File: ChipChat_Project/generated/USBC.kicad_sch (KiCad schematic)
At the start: 4 parts

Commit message: 💾 snapshot 2026-02-23_00-19-22
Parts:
- added D1, D2, D3, D4, D5: TVS 5V, symbol SD05_SOD323
- added FB1: 120Ω@100MHz, symbol FerriteBead
- added J1: USB_C_Receptacle_USB2.0_16P, symbol USB_C_Receptacle_USB2.0_16P
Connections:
- net GND: now also D1.2 (A2), D2.2 (A2), D3.2 (A2), D4.2 (A2), D5.2 (A2), J1.A1 (GND), J1.A12 (GND), J1.B1 (GND), J1.B12 (GND), J1.S1 (SHIELD)
- net PP_5V_VBUS: now also D5.1 (A1), FB1.2, J1.A4 (VBUS), J1.A9 (VBUS), J1.B4 (VBUS), J1.B9 (VBUS)
- net USB_CC1: now also D4.1 (A1), J1.A5 (CC1)
- net USB_CC2: now also J1.B5 (CC2)
- new net PP_5V_SYS: FB1.1
- new net USB_DN: D1.1 (A1), D2.1 (A1), J1.A7 (D-), J1.B7 (D-)
- new net USB_DP: D3.1 (A1), J1.A6 (D+), J1.B6 (D+)

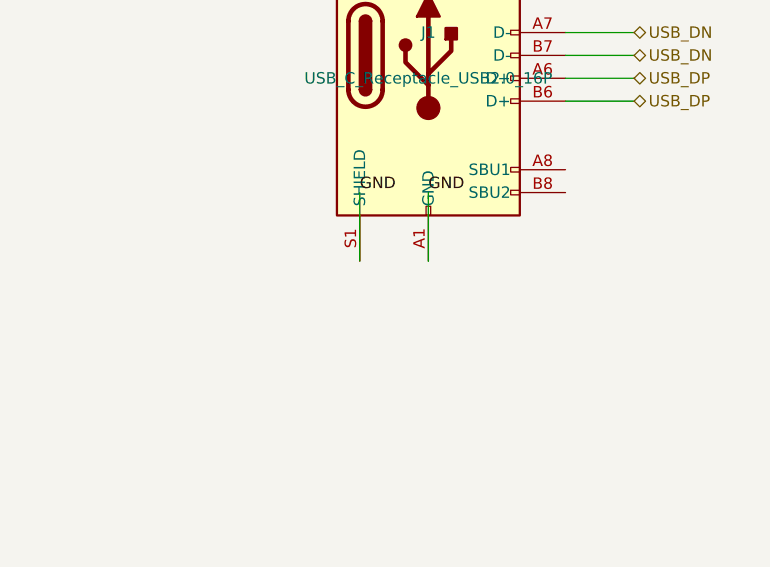
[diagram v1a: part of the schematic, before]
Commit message: finished basic full schematic generation from json, next follow and implement llm_integration.md
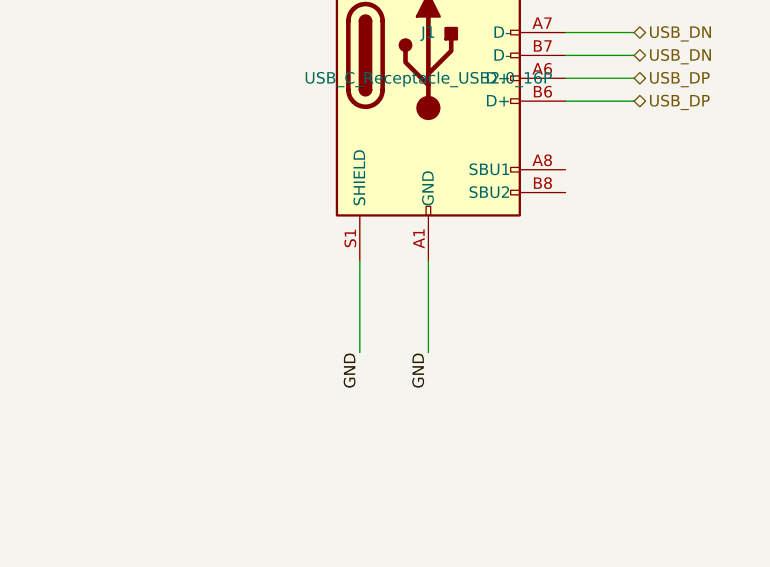
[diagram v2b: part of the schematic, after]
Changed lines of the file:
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@@
 	(wire
 		(pts
-			(xy 200.0 122.86) (xy 200.0 115.24)
+			(xy 200.0 122.86) (xy 200.0 133.02)
 		)
 		(stroke
@@
 	)
 	(label "GND"
-		(at 200.0 115.24 0)
+		(at 200.0 133.02 90)
 		(effects
 			(font
 				(size 1.27 1.27)
 			)
-			(justify left bottom)
+			(justify right bottom)
 		)
 	)
@@
 	(wire
 		(pts
-			(xy 192.38 122.86) (xy 192.38 115.24)
+			(xy 192.38 122.86) (xy 192.38 133.02)
 		)
 		(stroke
@@
 	)
 	(label "GND"
-		(at 192.38 115.24 0)
+		(at 192.38 133.02 90)
 		(effects
 			(font
 				(size 1.27 1.27)
 			)
-			(justify left bottom)
+			(justify right bottom)
 		)
 	)
